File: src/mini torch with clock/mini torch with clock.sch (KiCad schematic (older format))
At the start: 24 parts, among them J1 1-84953-4, J2 ICSP_HEADER, J3 UART_PROGRAMMER, Q1 YJL3407A, SW3 SW_Push, U1 DS3231MZ, U2 ATmega328P-AU

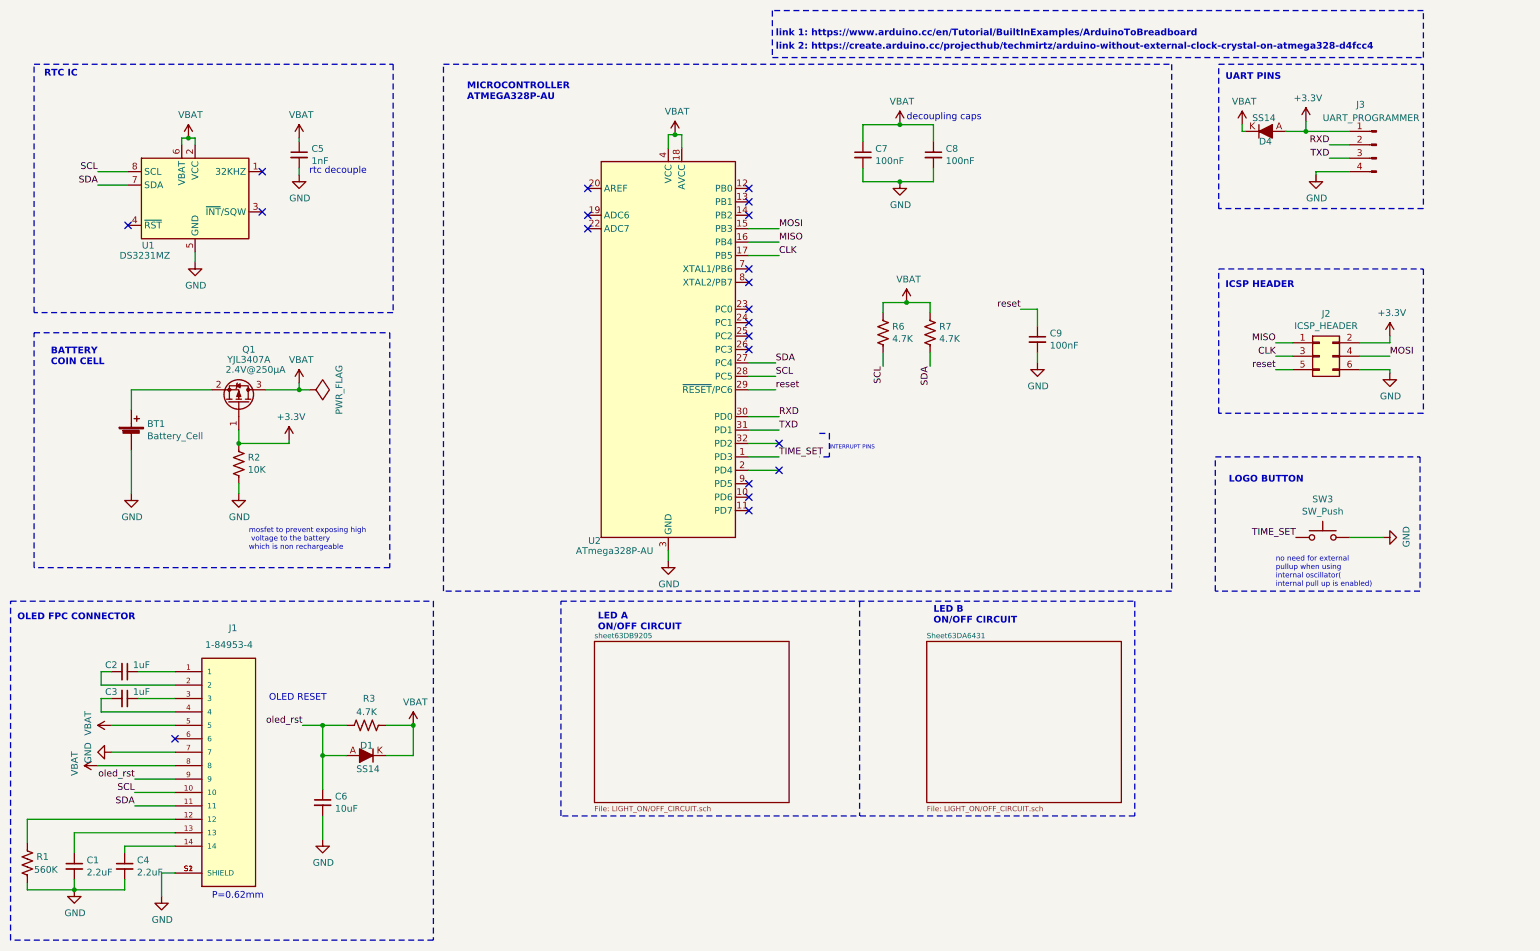
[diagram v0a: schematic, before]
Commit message: clock module complete awaiting PCB
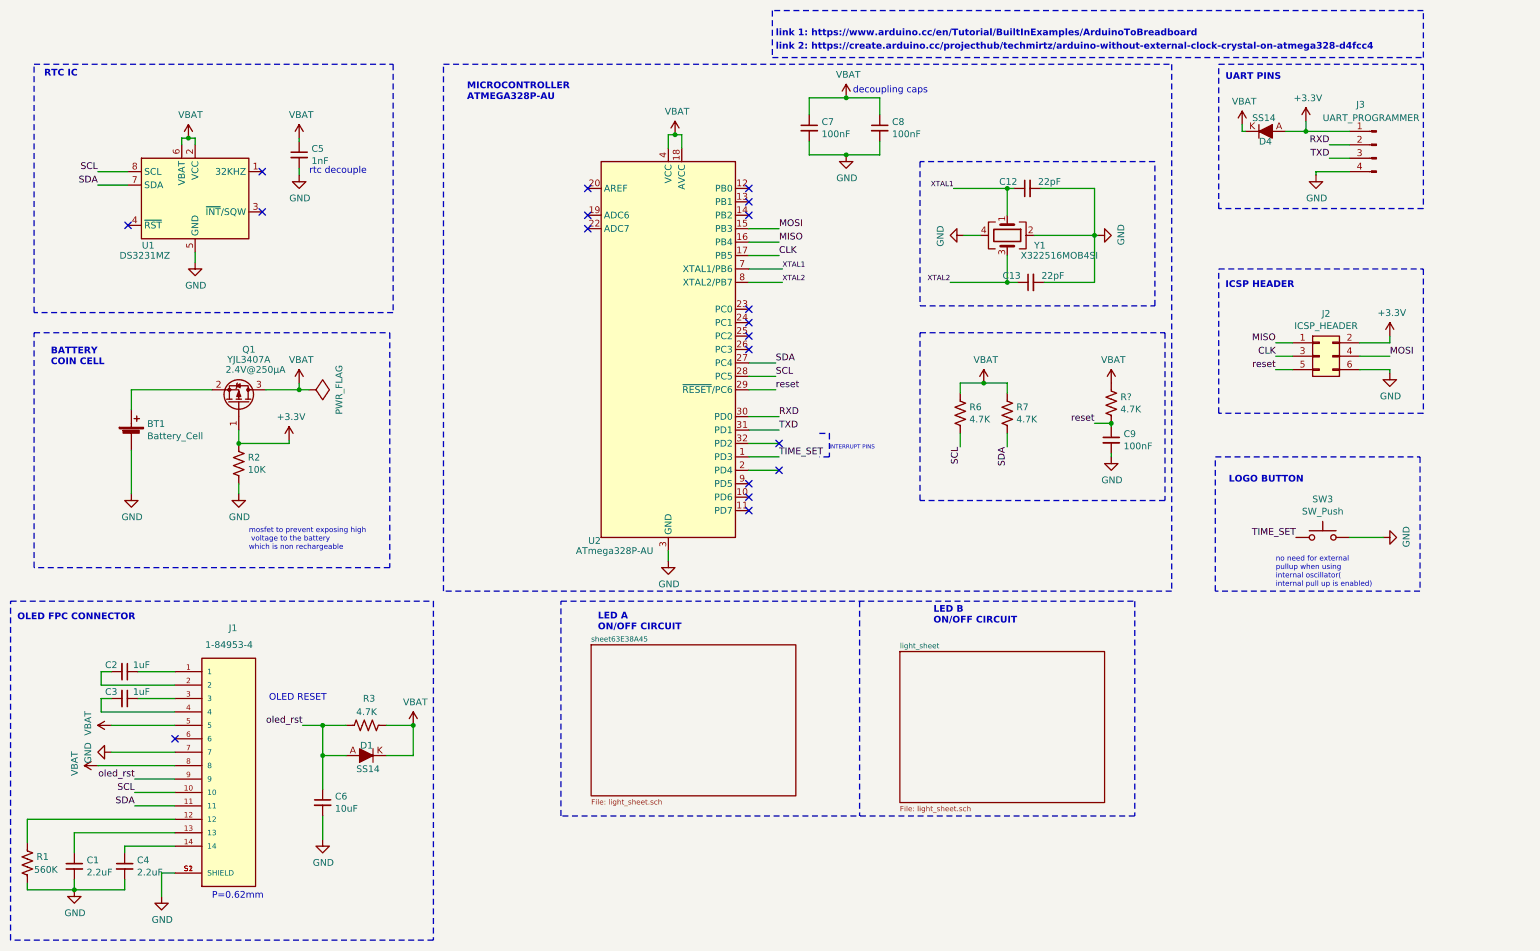
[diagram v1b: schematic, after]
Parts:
- added C12, C13: 22pF, Capacitor_SMD:C_0402_1005Metric, symbol Device:C_Small
- added R?: 4.7K, Resistor_SMD:R_0402_1005Metric, symbol Device:R_US
- added Y1: X322516MOB4SI, Crystal:Crystal_SMD_EuroQuartz_MT-4Pin_3.2x2.5mm, symbol Device:Crystal_GND24
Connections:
- net GND: now also C12.2, C13.2, Y1.2, Y1.4
- net VBAT: now also R?.1
- net reset: now also R?.2
- net XTAL1: now reaches U2.7 (XTAL1/PB6)
- net XTAL1: now also C12.1, Y1.1
- net XTAL2: now reaches U2.8 (XTAL2/PB7)
- net XTAL2: now also C13.1, Y1.3
- no-connect marks 21 -> 19
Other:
- moved on the sheet: C7, C8, C9, R6, R7
